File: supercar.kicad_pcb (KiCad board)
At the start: 2 copper layers, 63.5 x 43.6 mm, 41 parts, among them SW1 Power, U1 74HC283, U2 74HC574, U3 74HC154, U4 74HC574, U5 74HC86, U6 NE555D

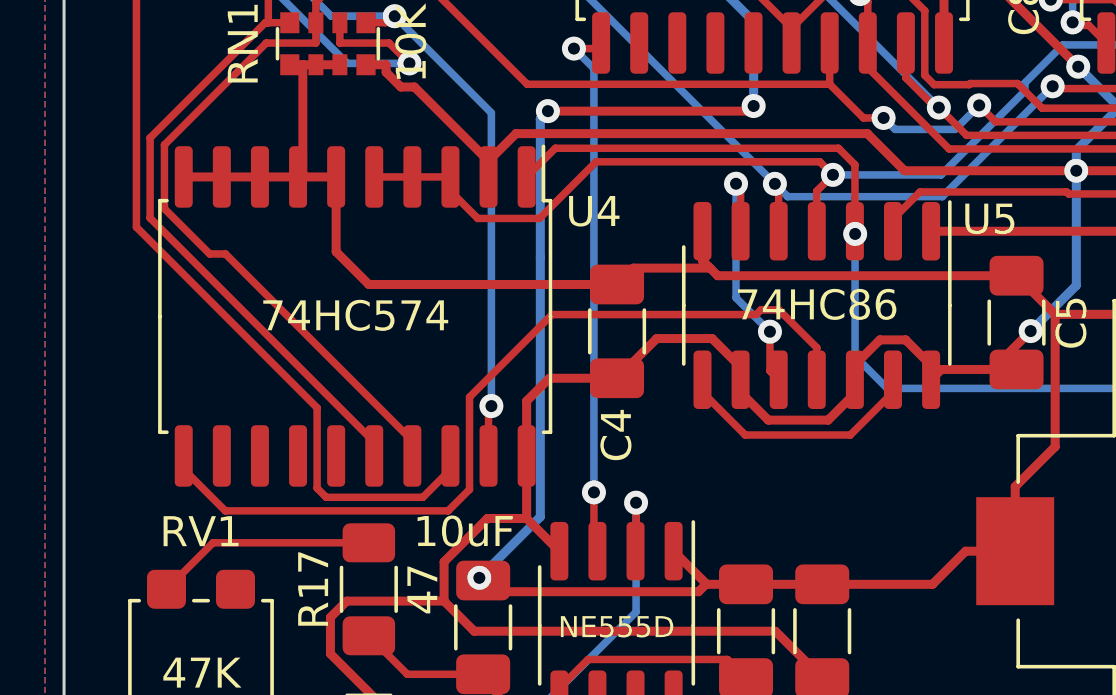
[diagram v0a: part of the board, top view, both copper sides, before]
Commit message: Feed the reset circuit on the delay line of the adder clock
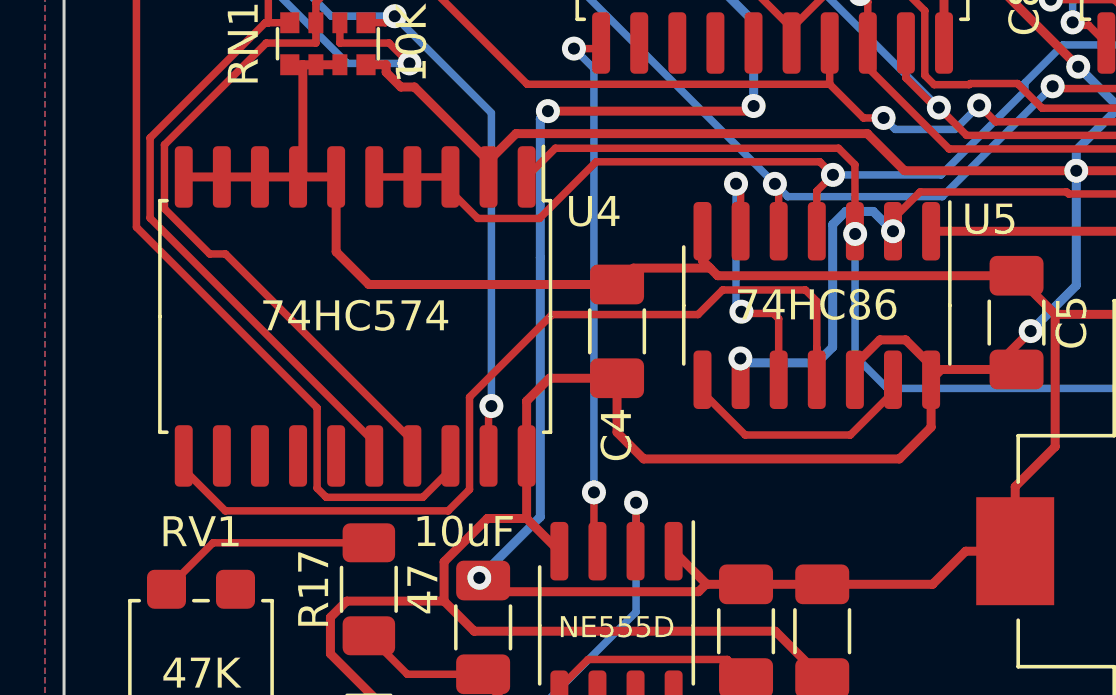
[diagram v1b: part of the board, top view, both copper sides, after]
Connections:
- C11 pad 1: Net-(D17-A) -> /~{RST}
- D17 pad 2: Net-(D17-A) -> /~{RST}
- R19 pad 1: Net-(D17-A) -> /~{RST}
- U5 pad 2: Net-(D17-A) -> /~{RST}
- U5 pad 9: +3V3 -> /~{RST}
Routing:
- net /~{RST}: track 0.00 -> 45.9 mm, vias 0 -> 2
- net Net-(D17-A): track 34.6 -> 0.00 mm
- net +3V3: track 249.0 -> 253.2 mm
- net Net-(U4-Cp): track 28.3 -> 30.8 mm
- net Net-(U5-Pad10): track 8.77 -> 9.36 mm

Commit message: Further changes to the board, changed the switch
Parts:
- SW1: footprint Button_Switch_THT:SW_Slide_1P2T_CK_OS102011MS2Q -> Button_Switch_SMD:SW_SPDT_CK-JS102011SAQN
- moved SW1 3.06 mm to (137.8, 56.8)
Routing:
- net +3V3: track 253.2 -> 249.8 mm, vias 3 -> 4
- net Net-(BT1-+): track 21.8 -> 25.2 mm, vias 1 -> 2
